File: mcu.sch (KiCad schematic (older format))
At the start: 29 parts, among them IC2 LPC55S16JBD64E, Y1 16 MHz, Y2 32.768 kHz

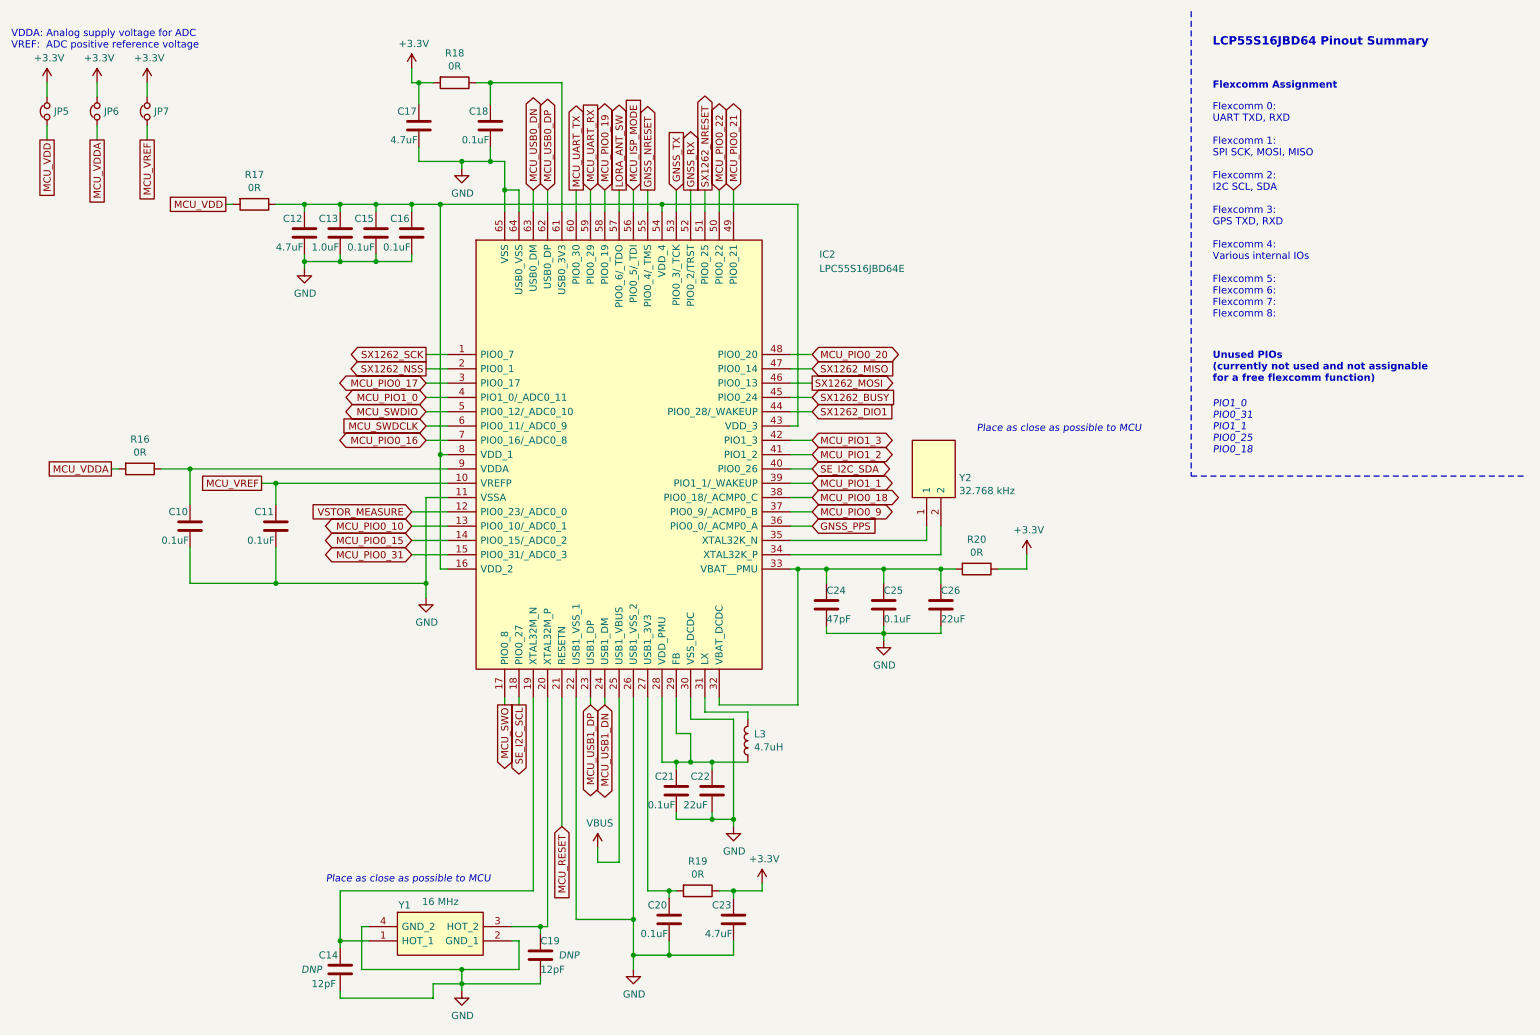
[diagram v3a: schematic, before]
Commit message: Removed jumpers from mcu
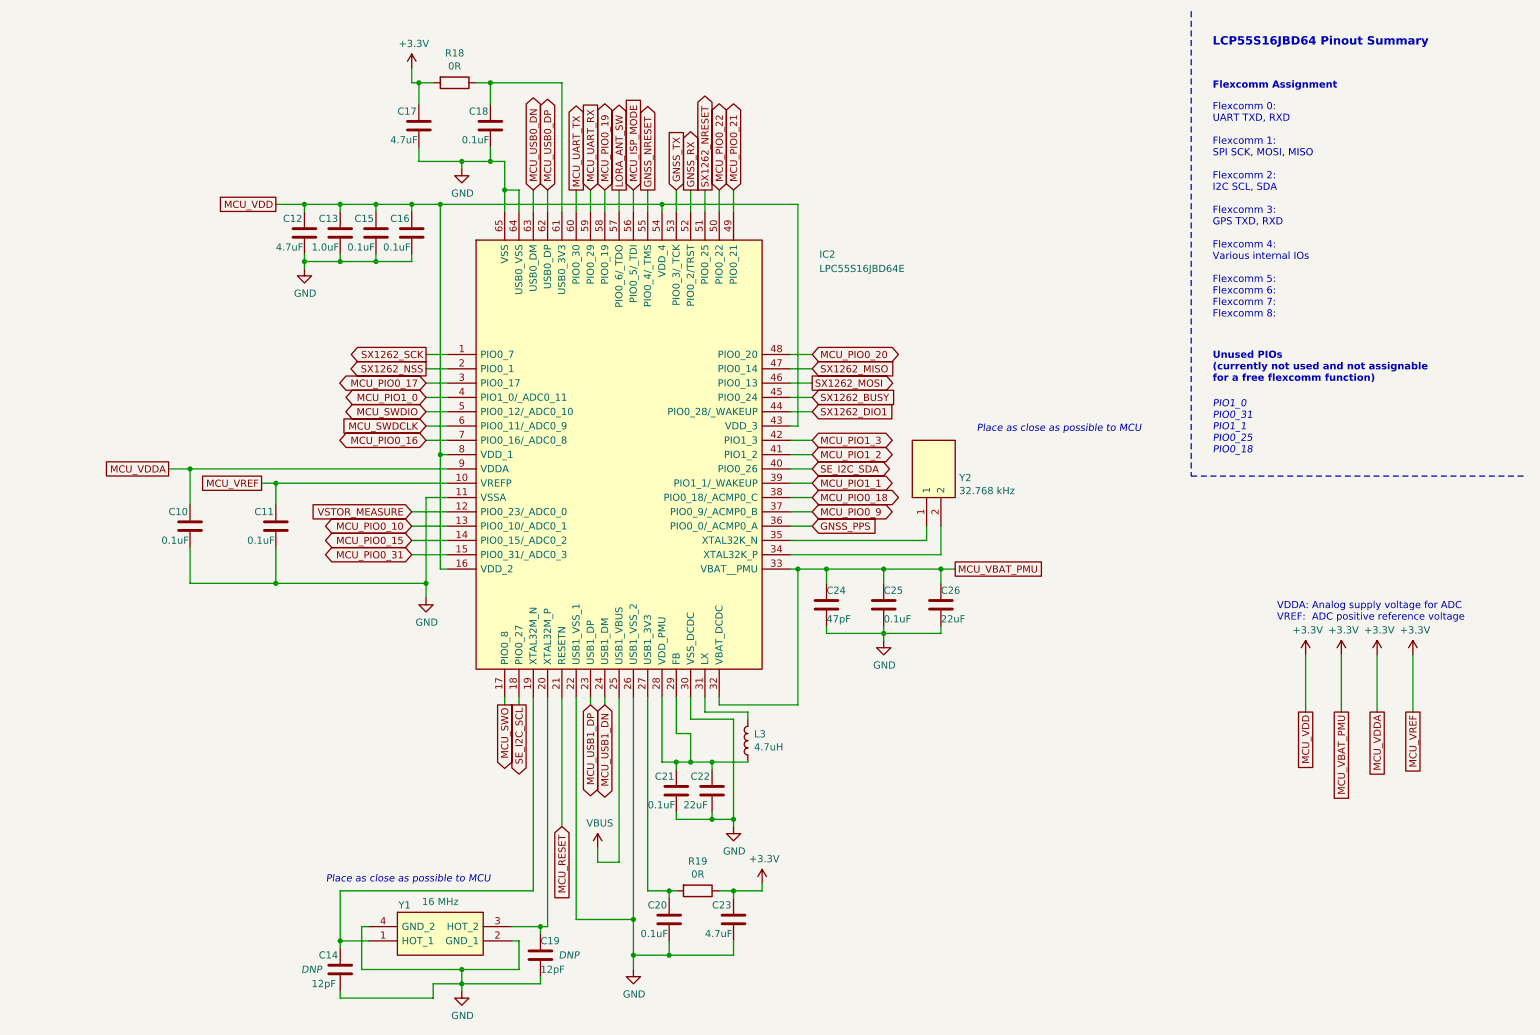
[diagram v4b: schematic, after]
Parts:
- removed JP5, JP6, JP7: Jumper_NC_Small, Jumper:SolderJumper-2_P1.3mm_Bridged_Pad1.0x1.5mm, symbol Device:Jumper_NC_Small
- removed R16, R17, R20: 0R, Resistor_SMD:R_0402_1005Metric, symbol Device:R
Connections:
- net MCU_VREF is gone; now on net +3V3: C11.1, IC2.10 (VREFP)
- net +3V3: now also C10.1, C12.1, C13.1, C15.1, C16.1, C24.1, C25.1, C26.1, IC2.16 (VDD_2), IC2.32 (VBAT_DCDC), IC2.33 (VBAT__PMU), IC2.43 (VDD_3), IC2.54 (VDD_4), IC2.8 (VDD_1), IC2.9 (VDDA)
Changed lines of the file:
@@
 	1    0    0    -1
 $EndComp
-Text GLabel 2050 1850 0    50   UnSpc ~ 0
+Text GLabel 2400 1850 0    50   UnSpc ~ 0
 MCU_VDD
 Wire Wire Line
@@
 Wire Wire Line
 	1800 3700 1800 3950
-Text GLabel 1250 3700 0    50   UnSpc ~ 0
+Text GLabel 1650 3700 0    50   UnSpc ~ 0
 MCU_VDDA
 Connection ~ 1800 3700
@@
 Wire Wire Line
 	1800 4250 1800 4500
-$Comp
-L Device:Jumper_NC_Small JP5
-U 1 1 5F7DD754
-P 800 1200
-F 0 "JP5" V 800 1152 50  0000 R CNN
-F 1 "Jumper_NC_Small" V 755 1153 50  0001 R CNN
-F 2 "Jumper:SolderJumper-2_P1.3mm_Bridged_Pad1.0x1.5mm" H 800 1200 50  0001 C CNN
-F 3 "~" H 800 1200 50  0001 C CNN
-	1    800  1200
-	0    -1   -1   0
-$EndComp
-Wire Wire Line
-	800  1000 800  1100
-Text GLabel 800  1400 3    50   UnSpc ~ 0
+Text GLabel 9600 5400 3    50   UnSpc ~ 0
 MCU_VDD
-Wire Wire Line
-	800  1400 800  1300
-$Comp
-L Device:Jumper_NC_Small JP6
-U 1 1 5F7E73B1
-P 1150 1200
-F 0 "JP6" V 1150 1152 50  0000 R CNN
-F 1 "Jumper_NC_Small" V 1105 1153 50  0001 R CNN
-F 2 "Jumper:SolderJumper-2_P1.3mm_Bridged_Pad1.0x1.5mm" H 1150 1200 50  0001 C CNN
-F 3 "~" H 1150 1200 50  0001 C CNN
-	1    1150 1200
-	0    -1   -1   0
-$EndComp
-Wire Wire Line
-	1150 1400 1150 1300
-$Comp
-L Device:Jumper_NC_Small JP7
-U 1 1 5F7EB320
-P 1500 1200
-F 0 "JP7" V 1500 1152 50  0000 R CNN
-F 1 "Jumper_NC_Small" V 1455 1153 50  0001 R CNN
-F 2 "Jumper:SolderJumper-2_P1.3mm_Bridged_Pad1.0x1.5mm" H 1500 1200 50  0001 C CNN
-F 3 "~" H 1500 1200 50  0001 C CNN
-	1    1500 1200
-	0    -1   -1   0
-$EndComp
-Wire Wire Line
-	1500 1000 1500 1100
-Wire Wire Line
-	1500 1400 1500 1300
-Text GLabel 1150 1400 3    50   UnSpc ~ 0
+Text GLabel 10100 5400 3    50   UnSpc ~ 0
 MCU_VDDA
 $Comp
@@
 Wire Wire Line
 	3450 3500 3600 3500
-Text GLabel 1500 1400 3    50   UnSpc ~ 0
+Text GLabel 10350 5400 3    50   UnSpc ~ 0
 MCU_VREF
 Text GLabel 3450 3500 0    50   BiDi ~ 0
@@
 Text Notes 2750 6600 0    50   Italic 0
 Place as close as possible to MCU
-Text Notes 550  850  0    50   ~ 0
+Text Notes 9400 4850 0    50   ~ 0
 VDDA: Analog supply voltage for ADC\nVREF:  ADC positive reference voltage\n\n
 $Comp
 L power:+3.3V #PWR020
 U 1 1 5F814958
-P 800 1000
-F 0 "#PWR020" H 800 850 50  0001 C CNN
-F 1 "+3.3V" H 815 1173 50  0000 C CNN
-F 2 "" H 800 1000 50  0001 C CNN
-F 3 "" H 800 1000 50  0001 C CNN
-	1    800  1000
+P 9600 5000
+F 0 "#PWR020" H 9600 4850 50  0001 C CNN
+F 1 "+3.3V" H 9615 5173 50  0000 C CNN
+F 2 "" H 9600 5000 50  0001 C CNN
+F 3 "" H 9600 5000 50  0001 C CNN
+	1    9600 5000
 	1    0    0    -1
 $EndComp
@@
 L power:+3.3V #PWR021
 U 1 1 5F814F31
-P 1150 1000
-F 0 "#PWR021" H 1150 850 50  0001 C CNN
-F 1 "+3.3V" H 1165 1173 50  0000 C CNN
-F 2 "" H 1150 1000 50  0001 C CNN
-F 3 "" H 1150 1000 50  0001 C CNN
-	1    1150 1000
+P 10100 5000
+F 0 "#PWR021" H 10100 4850 50  0001 C CNN
+F 1 "+3.3V" H 10115 5173 50  0000 C CNN
+F 2 "" H 10100 5000 50  0001 C CNN
+F 3 "" H 10100 5000 50  0001 C CNN
+	1    10100 5000
 	1    0    0    -1
 $EndComp
@@
 L power:+3.3V #PWR022
 U 1 1 5F81543D
-P 1500 1000
-F 0 "#PWR022" H 1500 850 50  0001 C CNN
-F 1 "+3.3V" H 1515 1173 50  0000 C CNN
-F 2 "" H 1500 1000 50  0001 C CNN
-F 3 "" H 1500 1000 50  0001 C CNN
-	1    1500 1000
-	1    0    0    -1
-$EndComp
-Wire Wire Line
-	1150 1000 1150 1100
+P 10350 5000
+F 0 "#PWR022" H 10350 4850 50  0001 C CNN
+F 1 "+3.3V" H 10365 5173 50  0000 C CNN
+F 2 "" H 10350 5000 50  0001 C CNN
+F 3 "" H 10350 5000 50  0001 C CNN
+	1    10350 5000
+	1    0    0    -1
+$EndComp
 Wire Wire Line
 	6000 4300 7050 4300
 Wire Wire Line
 	6000 4200 6950 4200
-$Comp
-L power:+3.3V #PWR033
-U 1 1 5F97F3C4
-P 7650 4300
-F 0 "#PWR033" H 7650 4150 50  0001 C CNN
-F 1 "+3.3V" H 7665 4473 50  0000 C CNN
-F 2 "" H 7650 4300 50  0001 C CNN
-F 3 "" H 7650 4300 50  0001 C CNN
-	1    7650 4300
-	1    0    0    -1
-$EndComp
-$Comp
-L Device:R R20
-U 1 1 5F97FCBC
-P 7300 4400
-F 0 "R20" V 7093 4400 50  0000 C CNN
-F 1 "0R" V 7184 4400 50  0000 C CNN
-F 2 "Resistor_SMD:R_0402_1005Metric" V 7230 4400 50  0001 C CNN
-F 3 "~" H 7300 4400 50  0001 C CNN
-	1    7300 4400
-	0    1    1    0
-$EndComp
-Wire Wire Line
-	7650 4300 7650 4400
-Wire Wire Line
-	7650 4400 7450 4400
-Wire Wire Line
-	7150 4400 7050 4400
 Connection ~ 7050 4400
-$Comp
-L Device:R R16
-U 1 1 5F994D9B
-P 1450 3700
-F 0 "R16" V 1243 3700 50  0000 C CNN
-F 1 "0R" V 1334 3700 50  0000 C CNN
-F 2 "Resistor_SMD:R_0402_1005Metric" V 1380 3700 50  0001 C CNN
-F 3 "~" H 1450 3700 50  0001 C CNN
-	1    1450 3700
-	0    1    1    0
-$EndComp
-Wire Wire Line
-	1250 3700 1300 3700
-Wire Wire Line
-	1600 3700 1800 3700
-$Comp
-L Device:R R17
-U 1 1 5F9AA32C
-P 2250 1850
-F 0 "R17" V 2043 1850 50  0000 C CNN
-F 1 "0R" V 2134 1850 50  0000 C CNN
-F 2 "Resistor_SMD:R_0402_1005Metric" V 2180 1850 50  0001 C CNN
-F 3 "~" H 2250 1850 50  0001 C CNN
-	1    2250 1850
-	0    1    1    0
-$EndComp
-Wire Wire Line
-	2400 1850 2600 1850
-Connection ~ 2600 1850
-Wire Wire Line
-	2100 1850 2050 1850
 $Comp
 L Device:C C21
@@
 	1    0    0    -1
 $EndComp
+Text GLabel 3350 4000 0    50   Input ~ 0
+VSTOR_MEASURE
+Wire Wire Line
+	5400 5400 5700 5400
+Wire Wire Line
+	5200 5750 5200 5800
+Wire Wire Line
+	5100 5300 5100 5750
+Wire Wire Line
+	5100 5750 5200 5750
+Connection ~ 5200 5750
+Wire Wire Line
+	5450 5800 5450 5750
+Connection ~ 5450 5750
+Wire Wire Line
+	5200 5750 5300 5750
+Wire Wire Line
+	5200 5300 5200 5550
+Wire Wire Line
+	5200 5550 5300 5550
+Wire Wire Line
+	5300 5550 5300 5750
+Connection ~ 5300 5750
+Wire Wire Line
+	5300 5750 5450 5750
+Wire Wire Line
+	5600 6200 5600 6150
+Wire Wire Line
+	5600 5450 5300 5450
+Wire Wire Line
+	5300 5450 5300 5300
+Wire Wire Line
+	5200 6100 5200 6150
+Wire Wire Line
+	5200 6150 5450 6150
+Connection ~ 5600 6150
+Wire Wire Line
+	5600 6150 5600 5450
+Wire Wire Line
+	5450 6100 5450 6150
+Connection ~ 5450 6150
+Wire Wire Line
+	5450 6150 5600 6150
+Text GLabel 3450 3100 0    50   BiDi ~ 0
+MCU_PIO0_17
+Wire Wire Line
+	9600 5000 9600 5400
+Wire Wire Line
+	10100 5000 10100 5400
+Wire Wire Line
+	10350 5000 10350 5400
+Text GLabel 9850 5400 3    50   UnSpc ~ 0
+MCU_VBAT_PMU
+$Comp
+L power:+3.3V #PWR?
+U 1 1 5FB0F073
+P 9850 5000
+F 0 "#PWR?" H 9850 4850 50  0001 C CNN
+F 1 "+3.3V" H 9865 5173 50  0000 C CNN
+F 2 "" H 9850 5000 50  0001 C CNN
+F 3 "" H 9850 5000 50  0001 C CNN
+	1    9850 5000
+	1    0    0    -1
+$EndComp
+Wire Wire Line
+	9850 5000 9850 5400
+Wire Wire Line
+	2400 1850 2600 1850
+Connection ~ 2600 1850
+Wire Wire Line
+	1650 3700 1800 3700
+Wire Wire Line
+	5700 5400 5700 5450
+Wire Wire Line
+	5450 5750 5700 5750
 $Comp
 L Device:L L3
@@
 	-1   0    0    1
 $EndComp
-Text GLabel 3350 4000 0    50   Input ~ 0
-VSTOR_MEASURE
-Wire Wire Line
-	5700 5400 5700 5450
-Wire Wire Line
-	5400 5400 5700 5400
-Wire Wire Line
-	5200 5750 5200 5800
-Wire Wire Line
-	5100 5300 5100 5750
-Wire Wire Line
-	5100 5750 5200 5750
-Connection ~ 5200 5750
-Wire Wire Line
-	5450 5800 5450 5750
-Connection ~ 5450 5750
-Wire Wire Line
-	5450 5750 5700 5750
-Wire Wire Line
-	5200 5750 5300 5750
-Wire Wire Line
-	5200 5300 5200 5550
-Wire Wire Line
-	5200 5550 5300 5550
-Wire Wire Line
-	5300 5550 5300 5750
-Connection ~ 5300 5750
-Wire Wire Line
-	5300 5750 5450 5750
-Wire Wire Line
-	5600 6200 5600 6150
-Wire Wire Line
-	5600 5450 5300 5450
-Wire Wire Line
-	5300 5450 5300 5300
-Wire Wire Line
-	5200 6100 5200 6150
-Wire Wire Line
-	5200 6150 5450 6150
-Connection ~ 5600 6150
-Wire Wire Line
-	5600 6150 5600 5450
-Wire Wire Line
-	5450 6100 5450 6150
-Connection ~ 5450 6150
-Wire Wire Line
-	5450 6150 5600 6150
-Text GLabel 3450 3100 0    50   BiDi ~ 0
-MCU_PIO0_17
+Text GLabel 7150 4400 2    50   UnSpc ~ 0
+MCU_VBAT_PMU
+Wire Wire Line
+	7050 4400 7150 4400
 $EndSCHEMATC

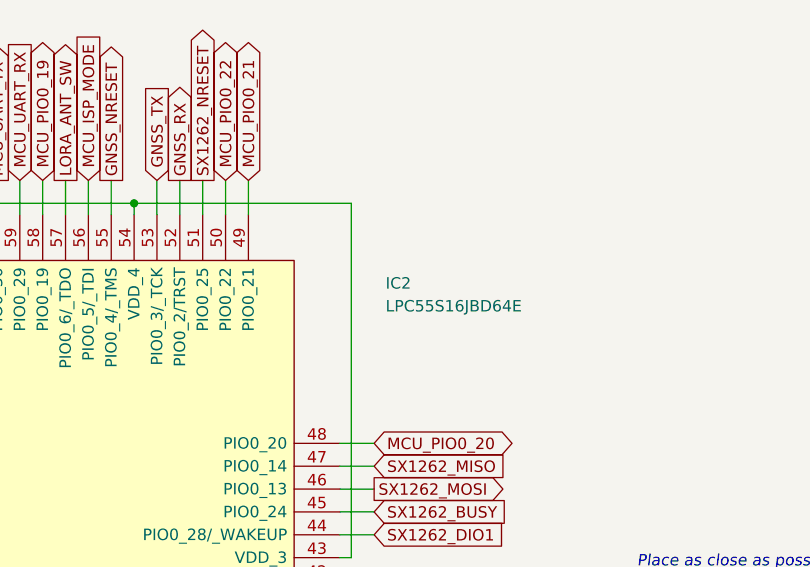
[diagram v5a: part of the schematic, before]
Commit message: Changed all symbols names from IC to U
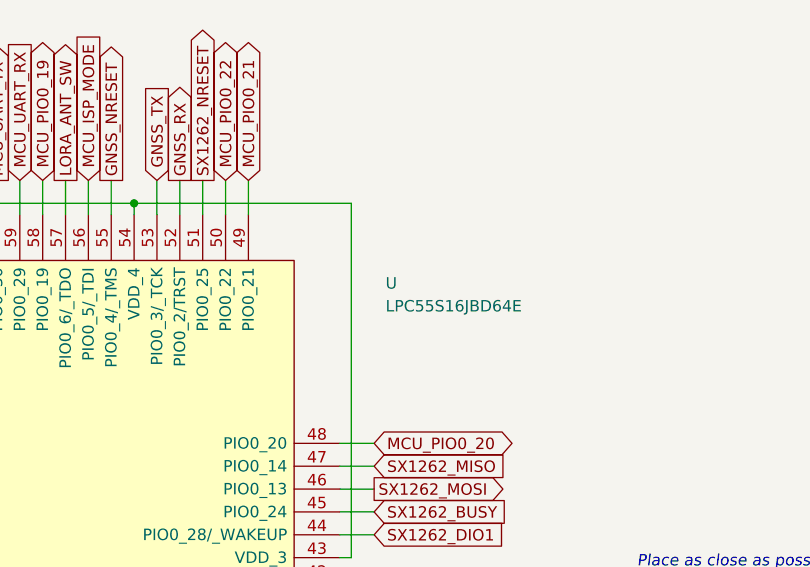
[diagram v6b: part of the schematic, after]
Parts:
- renumbered IC2 to U
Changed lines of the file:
@@
 P 3600 2900
 AR Path="/5F6D8582" Ref="IC?"  Part="1"
-AR Path="/5F6D82DD/5F6D8582" Ref="IC2"  Part="1"
-F 0 "IC2" H 6200 3600 50  0000 L CNN
+AR Path="/5F6D82DD/5F6D8582" Ref="U"  Part="1"
+F 0 "U" H 6200 3600 50  0000 L CNN
 F 1 "LPC55S16JBD64E" H 6200 3500 50  0000 L CNN
 F 2 "tardigrade-components:QFP50P1200X1200X120-65N" H 5850 3700 50  0001 L CNN

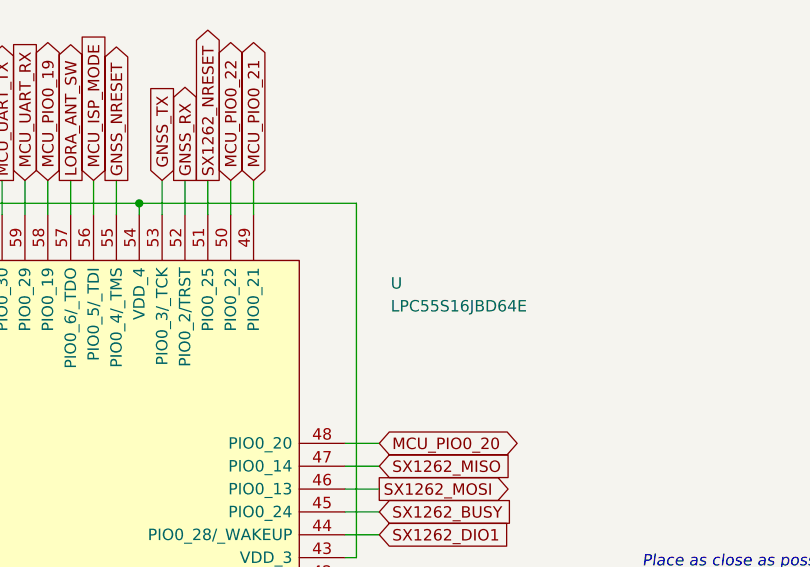
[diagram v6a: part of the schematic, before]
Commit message: Unnecessary note removed
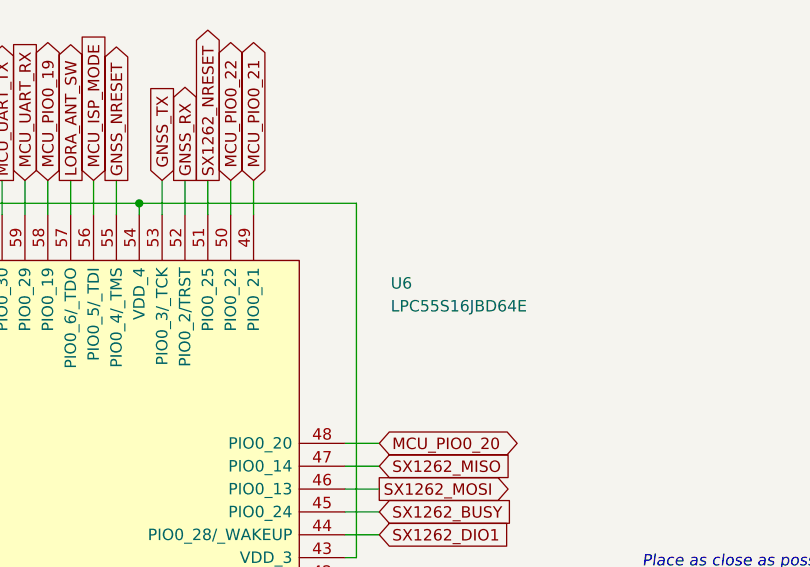
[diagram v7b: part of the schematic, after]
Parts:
- renumbered U to U6
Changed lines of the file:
@@
 P 3600 2900
 AR Path="/5F6D8582" Ref="IC?"  Part="1"
-AR Path="/5F6D82DD/5F6D8582" Ref="U"  Part="1"
-F 0 "U" H 6200 3600 50  0000 L CNN
+AR Path="/5F6D82DD/5F6D8582" Ref="U6"  Part="1"
+F 0 "U6" H 6200 3600 50  0000 L CNN
 F 1 "LPC55S16JBD64E" H 6200 3500 50  0000 L CNN
 F 2 "tardigrade-components:QFP50P1200X1200X120-65N" H 5850 3700 50  0001 L CNN
